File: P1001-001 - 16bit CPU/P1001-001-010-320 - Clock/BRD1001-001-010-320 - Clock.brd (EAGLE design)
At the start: 200 x 48 mm, 15 parts, among them IC1 74HC192D, IC12 74AC245DW, IC2 74HC192D, IC27 MEGA8535-A, IC3 74HC192D, IC4 74HC192D, IC7 74AC245DW, J1 22-27-2041-04

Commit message: Finish ALI Counter
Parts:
- removed BOTTOMBUS, FRONTBUS: (no value), con-harting-ml:ML16
- removed IC1, IC2: 74HC192D, 74xx-eu:SO16
- removed IC12, IC7: 74AC245DW, 74xx-eu:SO20W
- removed IC27: MEGA8535-A, atmel:TQFP44
- removed J1: 22-27-2041-04, con-molex:6410-04
- removed JP2: (no value), jumper:JP4
- removed RN2: (no value), resistor-dil:SOMC20
- removed SV5: (no value), con-harting-ml:ML6
- added !CLOCKPIN, VCC_GND1, VCC_GND2: (no value), con-harting-ml:ML16
- added C1, C5, C6: .01uF, rcl:C1206
- added C2: 1uF, rcl:C1206
- added C7: .1uF, rcl:C1206
- added CN1: (no value), adafruit:DCJACK_2MM_PTH
- added IC5: 74LS32D, 74xx-us:SO14
- added JP1: (no value), jumper:JP2
- added LED1: (no value), led:LED5MM
- added R1, R2, R4, R5, R7: 1k, rcl:M1206
- added R3: 1M, rcl:M1206
- added R6: (no value), rcl:M1206
- added S1: (no value), switch-omron:B3F-40XX
- added U$10, U$11, U$12, U$5, U$6, U$7, U$8, U$9: AZ1117E, 16bit:AZ1117E
- added U$2, U$3, U$4: NA555, 16bit:SO8
- IC3: value 74HC192D -> 74ALS04D; device 74xx-eu:SO16 -> 74xx-us:SO14
- IC4: value 74HC192D -> 74ALS08D; device 74xx-eu:SO16 -> 74xx-us:SO14
- U$1: value 4-DIGIT-7-SEGMENT -> 3310H-001-105L; device ADAFRUIT:4-DIGIT-7-SEGMENT -> 16bit:3310H-001-105L
- moved IC4 114.4 mm to (155.0, 33.0), turned to 0 degrees
- moved IC3 83.0 mm to (143.0, 32.0), flipped to the top, turned to 0 degrees
- moved U$1 76.8 mm to (151.0, 17.0)
- renumbered BACKBUS to CLOCKPIN
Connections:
- removed net !DEC: IC1.4, JP2.3
- removed net !INC: IC1.5, JP2.2
- removed net !REG_IN: IC1.11, IC2.11, IC3.11, IC4.11, JP2.1
- removed net !REG_OUT: IC12.19, IC7.19, JP2.4
- removed net A: IC27.37, RN2.20
- removed net B: IC27.36, RN2.19
- removed net BUS0: CLOCKPIN.1, FRONTBUS.1, IC1.9, IC12.9
- removed net BUS1: CLOCKPIN.2, FRONTBUS.2, IC1.10, IC12.8
- removed net BUS10: CLOCKPIN.11, FRONTBUS.11, IC3.1, IC7.7
- removed net BUS11: CLOCKPIN.12, FRONTBUS.12, IC3.15, IC7.6
- removed net BUS12: CLOCKPIN.13, FRONTBUS.13, IC4.9, IC7.5
- removed net BUS13: CLOCKPIN.14, FRONTBUS.14, IC4.10, IC7.4
- removed net BUS14: CLOCKPIN.15, FRONTBUS.15, IC4.1, IC7.3
- removed net BUS15: CLOCKPIN.16, FRONTBUS.16, IC4.15, IC7.2
- removed net BUS2: CLOCKPIN.3, FRONTBUS.3, IC1.1, IC12.7
- removed net BUS3: CLOCKPIN.4, FRONTBUS.4, IC1.15, IC12.6
- removed net BUS4: CLOCKPIN.5, FRONTBUS.5, IC12.5, IC2.9
- removed net BUS5: CLOCKPIN.6, FRONTBUS.6, IC12.4, IC2.10
- removed net BUS6: CLOCKPIN.7, FRONTBUS.7, IC12.3, IC2.1
- removed net BUS7: CLOCKPIN.8, FRONTBUS.8, IC12.2, IC2.15
- removed net BUS8: CLOCKPIN.9, FRONTBUS.9, IC3.9, IC7.9
- removed net BUS9: CLOCKPIN.10, FRONTBUS.10, IC3.10, IC7.8
- removed net C: IC27.35, RN2.18
- removed net CLEAR: IC1.14, IC2.14, IC3.14, IC4.14, J1.4
- removed net D: IC27.34, RN2.17
- removed net DIG0: IC27.40, U$1.PIN14
- removed net DIG1: IC27.41, U$1.PIN11
- removed net DIG2: IC27.42, U$1.PIN10
- removed net DIG3: IC27.43, U$1.PIN6
- removed net DP: IC27.30, RN2.13
- removed net E: IC27.33, RN2.16
- removed net F: IC27.32, RN2.15
- removed net G: IC27.31, RN2.14
- removed net N$18: IC27.1, SV5.3
- removed net N$19: IC27.3, SV5.4
- removed net N$20: IC27.2, SV5.6
- removed net N$21: IC27.4, SV5.2
- removed net N$24: RN2.1, U$1.PIN13
- removed net N$25: RN2.2, U$1.PIN9
- removed net N$26: RN2.3, U$1.PIN4
- removed net N$27: RN2.4, U$1.PIN2
- removed net N$28: RN2.5, U$1.PIN1
- removed net N$29: RN2.6, U$1.PIN12
- removed net N$30: RN2.7, U$1.PIN5
- removed net N$31: RN2.8, U$1.PIN3
- removed net N$7: IC3.13, IC4.4
- removed net SIGNAL0: BOTTOMBUS.1, IC1.7, IC12.11, IC27.9
- removed net SIGNAL1: BOTTOMBUS.2, IC1.6, IC12.12, IC27.10
- removed net SIGNAL10: BOTTOMBUS.11, IC27.21, IC3.2, IC7.13
- removed net SIGNAL11: BOTTOMBUS.12, IC27.22, IC3.3, IC7.14
- removed net SIGNAL12: BOTTOMBUS.13, IC27.23, IC4.7, IC7.15
- removed net SIGNAL13: BOTTOMBUS.14, IC27.24, IC4.6, IC7.16
- removed net SIGNAL14: BOTTOMBUS.15, IC27.25, IC4.2, IC7.17
- removed net SIGNAL15: BOTTOMBUS.16, IC27.26, IC4.3, IC7.18
- removed net SIGNAL2: BOTTOMBUS.3, IC1.2, IC12.13, IC27.11
- removed net SIGNAL3: BOTTOMBUS.4, IC1.3, IC12.14, IC27.12
- removed net SIGNAL4: BOTTOMBUS.5, IC12.15, IC2.7, IC27.13
- removed net SIGNAL5: BOTTOMBUS.6, IC12.16, IC2.6, IC27.14
- removed net SIGNAL6: BOTTOMBUS.7, IC12.17, IC2.2, IC27.15
- removed net SIGNAL7: BOTTOMBUS.8, IC12.18, IC2.3, IC27.16
- removed net SIGNAL8: BOTTOMBUS.9, IC27.19, IC3.7, IC7.11
- removed net SIGNAL9: BOTTOMBUS.10, IC27.20, IC3.6, IC7.12
- new net !CLK: !CLOCKPIN.1, !CLOCKPIN.10, !CLOCKPIN.11, !CLOCKPIN.12, !CLOCKPIN.13, !CLOCKPIN.14, !CLOCKPIN.15, !CLOCKPIN.16, !CLOCKPIN.2, !CLOCKPIN.3, !CLOCKPIN.4, !CLOCKPIN.5, !CLOCKPIN.6, !CLOCKPIN.7, !CLOCKPIN.8, !CLOCKPIN.9, IC3.6
- new net !HALT: IC4.10
- new net GNDBREAK: CN1.GNDBREAK
- new net IN: CN1.PWR, U$10.P$2, U$11.P$2, U$12.P$2, U$5.P$2, U$6.P$2, U$7.P$2, U$8.P$2, U$9.P$2
- new net N$10: C6.1, U$4.5
- new net N$11: C5.1, U$3.5
- new net N$12: IC3.1, IC4.1, U$4.3
- new net N$13: IC4.2, JP1.3, R1.1, R2.1, U$2.3
- new net N$14: IC4.4, U$3.3
- new net N$15: IC3.2, IC4.5
- new net N$16: IC4.3, IC5.1
- new net N$17: IC4.6, IC5.2
- new net N$22: IC4.9, IC5.3
- new net N$8: C2.1, U$1.P$3, U$2.2, U$2.6
- new net N$9: C1.1, U$2.5
- new net VCC1: S1.1, S1.2, U$3.2
- net CLK: now also CLOCKPIN.1, CLOCKPIN.10, CLOCKPIN.11, CLOCKPIN.12, CLOCKPIN.13, CLOCKPIN.14, CLOCKPIN.15, CLOCKPIN.16, CLOCKPIN.2, CLOCKPIN.3, CLOCKPIN.4, CLOCKPIN.5, CLOCKPIN.6, CLOCKPIN.7, CLOCKPIN.8, CLOCKPIN.9, IC3.5, IC4.8, LED1.A; no longer J1.3
- net GND: now also C1.2, C2.2, C5.2, C6.2, C7.2, CN1.GND, IC3.7, IC4.7, IC5.7, JP1.2, R6.1, U$10.P$1, U$11.P$1, U$12.P$1, U$2.1, U$3.1, U$4.1, U$4.6, U$5.P$1, U$6.P$1, U$7.P$1, U$8.P$1, U$9.P$1, VCC_GND1.1, VCC_GND1.11, VCC_GND1.13, VCC_GND1.15, VCC_GND1.3, VCC_GND1.5, VCC_GND1.7, VCC_GND1.9, VCC_GND2.1, VCC_GND2.11, VCC_GND2.13, VCC_GND2.15, VCC_GND2.3, VCC_GND2.5, VCC_GND2.7, VCC_GND2.9; no longer IC1.8, IC12.1, IC12.10, IC2.8, IC27.18, IC27.28, IC27.29, IC27.39, IC27.6, IC3.8, IC4.8, IC7.1, IC7.10, J1.1, SV5.1
- net N$1: now also R5.1, R7.1, U$2.7; no longer IC4.13
- net N$2: now also R7.2, U$1.P$2; no longer IC1.12, IC2.5
- net N$3: now also LED1.K, R6.2; no longer IC1.13, IC2.4
- net N$4: now also R2.2, U$4.2; no longer IC2.12, IC3.5
- net N$5: now also R4.2, S1.3, S1.4; no longer IC2.13, IC3.4
- net N$6: now also C7.1, R3.1, U$3.6, U$3.7; no longer IC3.12, IC4.5
- net VCC: now also IC3.14, IC4.14, IC5.14, JP1.1, R1.2, R3.2, R4.1, R5.2, U$10.P$3, U$11.P$3, U$12.P$3, U$2.4, U$2.8, U$3.4, U$3.8, U$4.4, U$4.8, U$5.P$3, U$6.P$3, U$7.P$3, U$8.P$3, U$9.P$3, VCC_GND1.10, VCC_GND1.12, VCC_GND1.14, VCC_GND1.16, VCC_GND1.2, VCC_GND1.4, VCC_GND1.6, VCC_GND1.8, VCC_GND2.10, VCC_GND2.12, VCC_GND2.14, VCC_GND2.16, VCC_GND2.2, VCC_GND2.4, VCC_GND2.6, VCC_GND2.8; no longer IC1.16, IC12.20, IC2.16, IC27.17, IC27.27, IC27.38, IC27.5, IC3.16, IC4.16, IC7.20, J1.2, SV5.5
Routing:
- net BUS1: track 269.3 -> 0.00 mm, vias 1 -> 0
- net BUS13: track 245.7 -> 0.00 mm
- net BUS8: track 241.9 -> 0.00 mm, vias 2 -> 0
- net BUS4: track 239.0 -> 0.00 mm, vias 4 -> 0
- net BUS5: track 237.6 -> 0.00 mm, vias 5 -> 0
- net BUS9: track 235.5 -> 0.00 mm, vias 5 -> 0
- net BUS15: track 230.7 -> 0.00 mm, vias 1 -> 0
- net BUS3: track 230.4 -> 0.00 mm, vias 1 -> 0
- net BUS11: track 226.0 -> 0.00 mm, vias 4 -> 0
- net BUS10: track 221.9 -> 0.00 mm, vias 5 -> 0
- net BUS2: track 221.7 -> 0.00 mm
- net BUS7: track 220.0 -> 0.00 mm, vias 2 -> 0
- net BUS6: track 218.8 -> 0.00 mm
- net BUS12: track 218.6 -> 0.00 mm
- net BUS0: track 213.2 -> 0.00 mm, vias 3 -> 0
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
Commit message: Check in the first try at soldering up the board
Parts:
- added AUTO, PULSE, SWITCH: NA555, 16bit:SO8
- added JP2: (no value), jumper:JP2
- added U$13: AZ1117E, 16bit:AZ1117E
- U$2, U$3, U$4: value NA555 -> AZ1117E; device 16bit:SO8 -> 16bit:AZ1117E
- moved U$4 97.3 mm to (27.0, 32.0)
- moved U$2 94.5 mm to (36.0, 15.0)
- moved U$3 93.6 mm to (36.0, 32.0)
- moved U$11 12.0 mm to (46.0, 15.0)
- moved U$12 11.0 mm to (45.0, 32.0)
- moved U$10 8.00 mm to (55.0, 15.0)
- moved U$9 8.00 mm to (55.0, 32.0)
- moved U$7 5.00 mm to (64.0, 15.0)
- moved U$8 5.00 mm to (64.0, 32.0)
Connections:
- removed net N$12: IC3.1, IC4.1, U$4.3
- removed net N$5 (its old number): R4.2, S1.3, S1.4
- removed net VCC1: S1.1, S1.2, U$3.2
- new net AUTOOUT: AUTO.3, IC4.1
- new net N$7: PULSE.2, R4.1, S1.1, S1.2
- new net PULSEOUT: IC4.4, PULSE.3
- new net SWITCHOUT: IC3.1, IC4.2, SWITCH.3
- net !HALT: now also JP2.3
- net GND: now also AUTO.1, PULSE.1, S1.3, S1.4, SWITCH.1, SWITCH.6, U$13.P$1, U$2.P$1, U$3.P$1, U$4.P$1; no longer C1.2, U$2.1, U$3.1, U$4.1, U$4.6
- net IN: now also U$13.P$2, U$2.P$2, U$3.P$2, U$4.P$2
- net N$1: now also AUTO.2, AUTO.6, C2.1, U$1.P$3; no longer R5.1, R7.1, U$2.7
- net N$10: now also PULSE.7, R3.1; no longer C6.1, U$4.5
- net N$11: now also C6.1, SWITCH.5; no longer C5.1, U$3.5
- net N$13: now also SWITCH.4; no longer IC4.2, R1.1, U$2.3
- net N$14: now also JP1.1, R1.1, SWITCH.2; no longer IC4.4, U$3.3
- net N$4: now also AUTO.5, C1.1; no longer R2.2, U$4.2
- net N$6: now also AUTO.7, R5.1, R7.1; no longer C7.1, R3.1, U$3.6, U$3.7
- net N$8: now also C7.1, PULSE.6; no longer C2.1, U$1.P$3, U$2.2, U$2.6
- net N$9: now also C5.1, PULSE.5; no longer C1.1, U$2.5
- net VCC: now also AUTO.4, AUTO.8, C1.2, PULSE.4, PULSE.8, R2.2, R4.2, SWITCH.8, U$13.P$3, U$2.P$3, U$3.P$3, U$4.P$3; no longer JP1.1, R4.1, U$2.4, U$2.8, U$3.4, U$3.8, U$4.4, U$4.8
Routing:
- net N$7: track 0.00 -> 77.6 mm, vias 0 -> 2
- net N$5 (its old number): track 64.5 -> 0.00 mm
- net VCC1: track 56.5 -> 0.00 mm, vias 1 -> 0
- net IN: track 115.4 -> 163.3 mm
- net SWITCHOUT: track 0.00 -> 47.2 mm, vias 0 -> 4
- net N$12: track 46.2 -> 0.00 mm, vias 2 -> 0
- net N$4: track 61.5 -> 18.0 mm
- net N$5: track 42.6 -> 83.1 mm
- net N$14: track 33.1 -> 73.4 mm, vias 0 -> 2
- net PULSEOUT: track 0.00 -> 34.2 mm, vias 0 -> 2
- net N$8: track 56.0 -> 22.5 mm, vias 3 -> 2
- net !HALT: track 0.00 -> 31.7 mm, vias 0 -> 1
- net AUTOOUT: track 0.00 -> 23.3 mm, vias 0 -> 2
- net N$13: track 79.9 -> 98.7 mm, vias 3 -> 1
- net GND: track 397.6 -> 412.7 mm, vias 3 -> 5
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
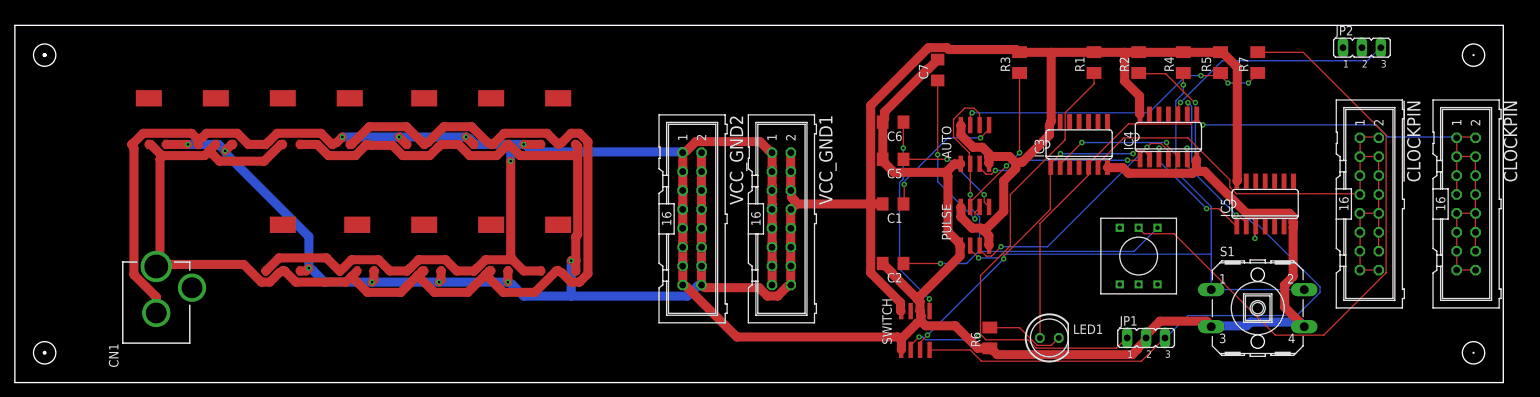
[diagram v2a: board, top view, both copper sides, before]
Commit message: add ram to Memory
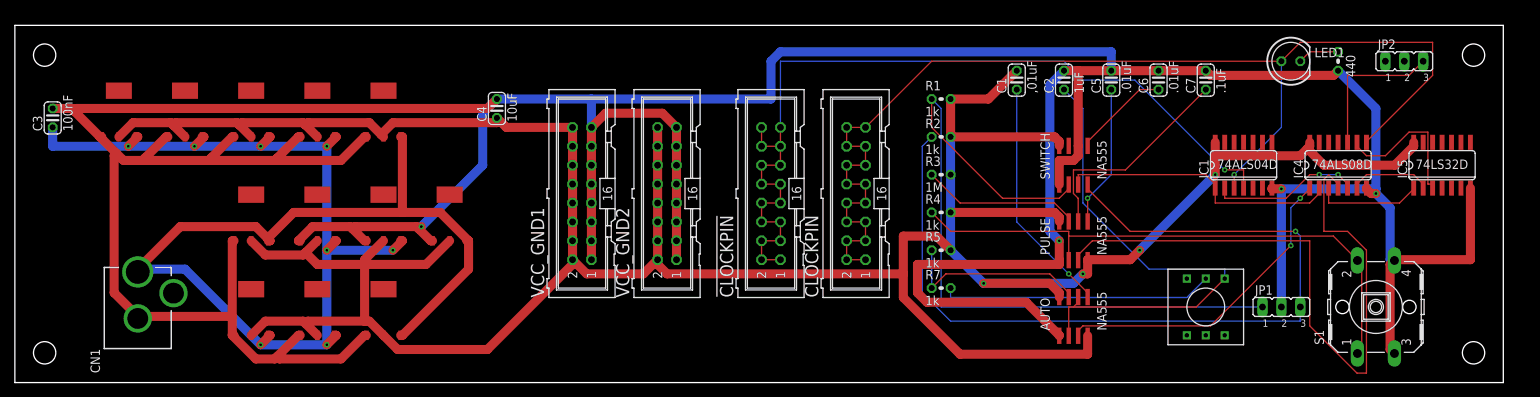
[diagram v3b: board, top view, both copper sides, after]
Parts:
- removed IC3: 74ALS04D, 74xx-us:SO14
- added C3: 100nF, rcl:C025-024X044
- added C4: 10uF, rcl:C025-024X044
- added IC1: 74ALS04D, 74xx-us:SO14
- C1: value .01uF -> ,01uF; device rcl:C1206 -> rcl:C025-024X044
- C2, C5, C6, C7: device rcl:C1206 -> rcl:C025-024X044
- R1, R2, R3, R4, R5, R7: device rcl:M1206 -> rcl:0204V
- R6: value (none) -> 440; device rcl:M1206 -> rcl:0204V
- U$10, U$11, U$12, U$13, U$2, U$3, U$4, U$5, U$6, U$7, U$8, U$9: value AZ1117E -> LD1117S33TR; device 16bit:AZ1117E -> P1001-001-310 - Eagle Library:AZ1117E
- moved CLOCKPIN 82.0 mm to (113.0, 25.4), turned to 90 degrees
- moved !CLOCKPIN 80.4 mm to (101.6, 25.4), turned to 90 degrees
- moved R6 59.8 mm to (177.8, 43.2)
- moved R7 52.2 mm to (124.5, 12.7), turned to 0 degrees
- moved LED1 49.3 mm to (171.4, 43.2)
- moved R5 45.2 mm to (124.5, 17.8), turned to 0 degrees
- moved U$5 43.2 mm to (31.8, 19.1)
- moved U$13 42.4 mm to (58.4, 19.1)
- moved U$6 42.1 mm to (31.8, 6.35)
- moved R4 38.3 mm to (124.5, 22.9), turned to 0 degrees
- moved U$10 36.8 mm to (22.9, 33.0)
- moved U$11 36.8 mm to (14.0, 33.0)
- moved C6 36.1 mm to (153.7, 40.6), turned to 90 degrees
- moved C7 36.0 mm to (160.0, 40.6)
- moved C2 33.7 mm to (141.0, 40.6), turned to 90 degrees
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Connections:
- net !CLK: now also IC1.4; no longer IC3.6
- net CLK: now also IC1.3; no longer IC3.5
- net GND: now also C3.2, C4.2, IC1.7; no longer IC3.7
- net IN: now also C3.1, U$10.P$3, U$11.P$3, U$12.P$3, U$13.P$3, U$2.P$3, U$3.P$3, U$4.P$3, U$5.P$3, U$6.P$3, U$7.P$3, U$8.P$3, U$9.P$3; no longer U$10.P$2, U$11.P$2, U$12.P$2, U$13.P$2, U$2.P$2, U$3.P$2, U$4.P$2, U$5.P$2, U$6.P$2, U$7.P$2, U$8.P$2, U$9.P$2
- net N$15: now also IC1.2; no longer IC3.2
- net SWITCHOUT: now also IC1.1; no longer IC3.1
- net VCC: now also C4.1, IC1.14, U$10.P$2, U$11.P$2, U$12.P$2, U$13.P$2, U$2.P$2, U$3.P$2, U$4.P$2, U$5.P$2, U$6.P$2, U$7.P$2, U$8.P$2, U$9.P$2; no longer IC3.14, U$10.P$3, U$11.P$3, U$12.P$3, U$13.P$3, U$2.P$3, U$3.P$3, U$4.P$3, U$5.P$3, U$6.P$3, U$7.P$3, U$8.P$3, U$9.P$3
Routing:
- net GND: track 412.7 -> 599.8 mm, vias 5 -> 4
- net VCC: track 371.0 -> 450.2 mm, vias 7 -> 4
- net PULSEOUT: track 34.2 -> 87.8 mm, vias 2 -> 0
- net N$5: track 83.1 -> 36.6 mm
- net !CLK: track 79.2 -> 118.5 mm, vias 0 -> 1
- net CLK: track 118.7 -> 155.8 mm
- net IN: track 163.3 -> 200.0 mm, vias 0 -> 8
- net N$14: track 73.4 -> 98.9 mm, vias 2 -> 0
- net AUTOOUT: track 23.3 -> 42.8 mm
- net N$13: track 98.7 -> 117.1 mm
- net N$6: track 43.7 -> 25.9 mm, vias 4 -> 0
- net N$11: track 27.3 -> 13.0 mm, vias 2 -> 0
- net N$4: track 18.0 -> 31.8 mm, vias 2 -> 1
- net !HALT: track 31.7 -> 19.9 mm, vias 1 -> 0
- net SWITCHOUT: track 47.2 -> 38.0 mm, vias 4 -> 0
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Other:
- board text added: "BRD1001-001-010-320 A Clock"
- board text added: "Copyright 2020 James Wright"
